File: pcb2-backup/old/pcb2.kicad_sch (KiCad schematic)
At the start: 69 parts, among them J1 WQP419GR_audio_in_1, J10 ACJS-HHOP_pedal_3, J11 ACJS-HHOP_pedal_4, J12 PMOD_JD, J13 PMOD_JC, J14 ACJS-HHOP_audio_out_L, J15 ACJS-HHOP_audio_out_R, J2 WQP419GR_audio_in_3, J3 Barrel_+5V_in, J4 Conn_+5V_to_FPGA, J5 Conn_GND_to_FPGA, J6 WQP419GR_audio_in_2, J7 WQP419GR_audio_in_4, J8 ACJS-HHOP_pedal_1, J9 ACJS-HHOP_pedal_2, U1 LM3940, U2 PCM1840, U3 ADC104S021, U4 TAD5242

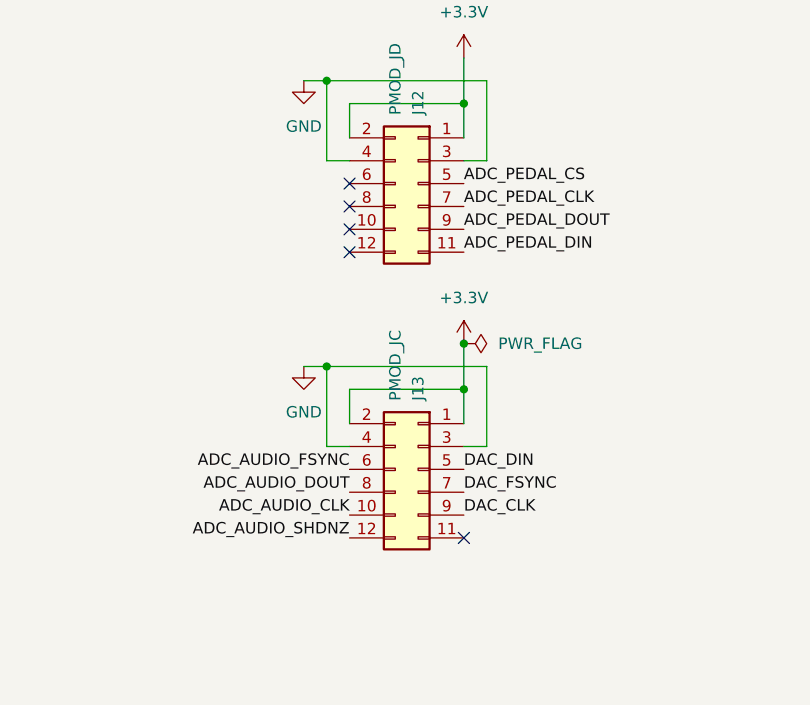
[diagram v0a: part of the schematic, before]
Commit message: Implement expression pedal controls
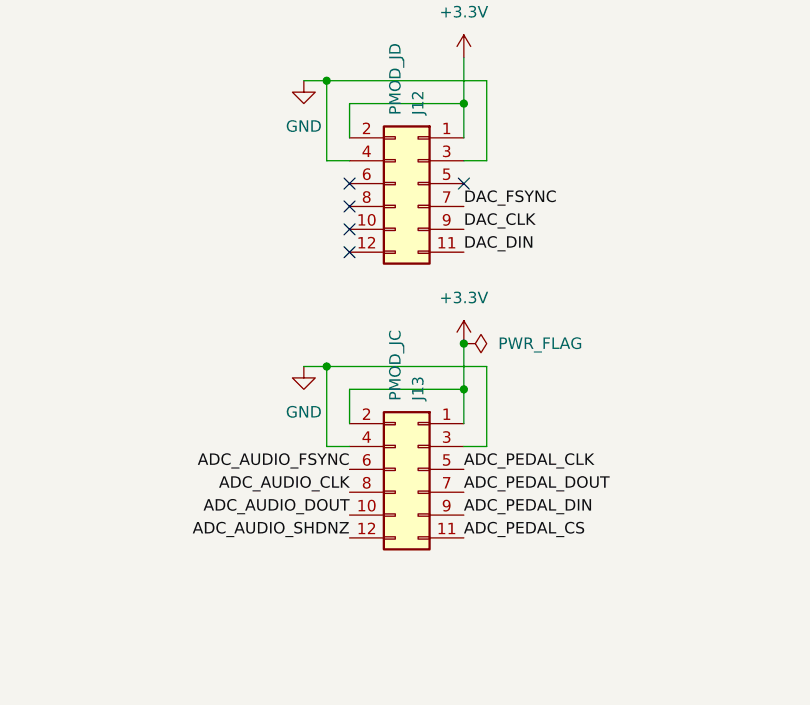
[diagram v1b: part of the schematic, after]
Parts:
- C10, C5, J1, J10, J11, J12, J13, J14, J15, J2, J3, J4, J5, J6, J7, J8, J9, U1: now in the parts list
- U3: FT Rotation Offset -90 -> (none)
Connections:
- net ADC_AUDIO_CLK: now also J13.8 (Pin_8); no longer J13.10 (Pin_10)
- net ADC_AUDIO_DOUT: now also J13.10 (Pin_10); no longer J13.8 (Pin_8)
- net ADC_PEDAL_CLK: now also J13.5 (Pin_5); no longer J12.7 (Pin_7)
- net ADC_PEDAL_CS: now also J13.11 (Pin_11); no longer J12.5 (Pin_5)
- net ADC_PEDAL_DIN: now also J13.9 (Pin_9); no longer J12.11 (Pin_11)
- net ADC_PEDAL_DOUT: now also J13.7 (Pin_7); no longer J12.9 (Pin_9)
- net DAC_CLK: now also J12.9 (Pin_9); no longer J13.9 (Pin_9)
- net DAC_DIN: now also J12.11 (Pin_11); no longer J13.5 (Pin_5)
- net DAC_FSYNC: now also J12.7 (Pin_7); no longer J13.7 (Pin_7)
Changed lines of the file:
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@@
 	)
 	(no_connect
-		(at 232.41 160.02)
+		(at 232.41 120.65)
 	)
 	(no_connect
@@
 		)
 	)
+	(label "ADC_PEDAL_CS"
+		(at 232.41 160.02 0)
+		(effects
+			(font
+				(size 1.27 1.27)
+			)
+			(justify left bottom)
+		)
+	)
 	(label "DAC_DIN"
-		(at 232.41 152.4 0)
+		(at 232.41 128.27 0)
 		(effects
 			(font
@@
 		)
 	)
-	(label "ADC_IN4N"
-		(at 100.33 148.59 0)
+	(label "ADC_PEDAL_DIN"
+		(at 232.41 157.48 0)
 		(effects
 			(font
@@
 		)
 	)
-	(label "DAC_OUT2N"
-		(at 246.38 80.01 0)
+	(label "ADC_IN4N"
+		(at 100.33 148.59 0)
 		(effects
 			(font
@@
 		)
 	)
-	(label "ADC_PEDAL_DOUT"
-		(at 166.37 46.99 0)
+	(label "ADC_PEDAL_CLK"
+		(at 232.41 152.4 0)
 		(effects
 			(font
@@
 		)
 	)
-	(label "ADC_PEDAL_CS"
-		(at 166.37 52.07 0)
+	(label "DAC_OUT2N"
+		(at 246.38 80.01 0)
 		(effects
 			(font
@@
 		)
 	)
-	(label "ADC_PEDAL_DIN"
-		(at 232.41 128.27 0)
+	(label "ADC_PEDAL_DOUT"
+		(at 166.37 46.99 0)
 		(effects
 			(font
@@
 	)
 	(label "ADC_PEDAL_CS"
-		(at 232.41 120.65 0)
+		(at 166.37 52.07 0)
 		(effects
 			(font
@@
 	)
 	(label "ADC_PEDAL_DOUT"
-		(at 232.41 125.73 0)
+		(at 232.41 154.94 0)
 		(effects
 			(font
@@
 	)
 	(label "ADC_AUDIO_CLK"
-		(at 219.71 157.48 180)
+		(at 219.71 154.94 180)
 		(effects
 			(font
@@
 	)
 	(label "DAC_FSYNC"
-		(at 232.41 154.94 0)
-		(effects
-			(font
-				(size 1.27 1.27)
-			)
-			(justify left bottom)
-		)
-	)
-	(label "ADC_PEDAL_CLK"
 		(at 232.41 123.19 0)
 		(effects
@@
 	)
 	(label "ADC_AUDIO_DOUT"
-		(at 219.71 154.94 180)
+		(at 219.71 157.48 180)
 		(effects
 			(font
@@
 	)
 	(label "DAC_CLK"
-		(at 232.41 157.48 0)
+		(at 232.41 125.73 0)
 		(effects
 			(font
@@
 		(body_style 1)
 		(exclude_from_sim no)
-		(in_bom no)
+		(in_bom yes)
 		(on_board yes)
-		(in_pos_files no)
+		(in_pos_files yes)
 		(dnp no)
 		(property "Reference" "J11"
@@
 		(body_style 1)
 		(exclude_from_sim no)
-		(in_bom no)
+		(in_bom yes)
 		(on_board yes)
-		(in_pos_files no)
+		(in_pos_files yes)
 		(dnp no)
 		(fields_autoplaced yes)
@@
 		(body_style 1)
 		(exclude_from_sim no)
-		(in_bom no)
+		(in_bom yes)
 		(on_board yes)
-		(in_pos_files no)
+		(in_pos_files yes)
 		(dnp no)
 		(property "Reference" "J4"
@@
 		(body_style 1)
 		(exclude_from_sim no)
-		(in_bom no)
+		(in_bom yes)
 		(on_board yes)
-		(in_pos_files no)
+		(in_pos_files yes)
 		(dnp no)
 		(fields_autoplaced yes)
@@
 		(body_style 1)
 		(exclude_from_sim no)
-		(in_bom no)
+		(in_bom yes)
 		(on_board yes)
-		(in_pos_files no)
+		(in_pos_files yes)
 		(dnp no)
 		(property "Reference" "J1"
@@
 		(body_style 1)
 		(exclude_from_sim no)
-		(in_bom no)
+		(in_bom yes)
 		(on_board yes)
-		(in_pos_files no)
+		(in_pos_files yes)
 		(dnp no)
 		(property "Reference" "J10"
@@
 		(body_style 1)
 		(exclude_from_sim no)
-		(in_bom no)
+		(in_bom yes)
 		(on_board yes)
-		(in_pos_files no)
+		(in_pos_files yes)
 		(dnp no)
 		(property "Reference" "J8"
@@
 		(body_style 1)
 		(exclude_from_sim no)
-		(in_bom no)
+		(in_bom yes)
 		(on_board yes)
-		(in_pos_files no)
+		(in_pos_files yes)
 		(dnp no)
 		(property "Reference" "J5"
@@
 		(body_style 1)
 		(exclude_from_sim no)
-		(in_bom no)
+		(in_bom yes)
 		(on_board yes)
-		(in_pos_files no)
+		(in_pos_files yes)
 		(dnp no)
 		(property "Reference" "J7"
@@
 		(body_style 1)
 		(exclude_from_sim no)
-		(in_bom no)
+		(in_bom yes)
 		(on_board yes)
-		(in_pos_files no)
+		(in_pos_files yes)
 		(dnp no)
 		(fields_autoplaced yes)
@@
 		(body_style 1)
 		(exclude_from_sim no)
-		(in_bom no)
+		(in_bom yes)
 		(on_board yes)
-		(in_pos_files no)
+		(in_pos_files yes)
 		(dnp no)
 		(property "Reference" "J15"
@@
 		(body_style 1)
 		(exclude_from_sim no)
-		(in_bom no)
+		(in_bom yes)
 		(on_board yes)
-		(in_pos_files no)
+		(in_pos_files yes)
 		(dnp no)
 		(property "Reference" "J13"
@@
 		(body_style 1)
 		(exclude_from_sim no)
-		(in_bom no)
+		(in_bom yes)
 		(on_board yes)
-		(in_pos_files no)
+		(in_pos_files yes)
 		(dnp no)
 		(property "Reference" "J9"
@@
 		(body_style 1)
 		(exclude_from_sim no)
-		(in_bom no)
+		(in_bom yes)
 		(on_board yes)
-		(in_pos_files no)
+		(in_pos_files yes)
 		(dnp no)
 		(property "Reference" "J2"
@@
 		(body_style 1)
 		(exclude_from_sim no)
-		(in_bom no)
+		(in_bom yes)
 		(on_board yes)
-		(in_pos_files no)
+		(in_pos_files yes)
 		(dnp no)
 		(property "Reference" "J12"
@@
 		(body_style 1)
 		(exclude_from_sim no)
-		(in_bom no)
+		(in_bom yes)
 		(on_board yes)
-		(in_pos_files no)
+		(in_pos_files yes)
 		(dnp no)
 		(property "Reference" "J14"
@@
 		(body_style 1)
 		(exclude_from_sim no)
-		(in_bom no)
+		(in_bom yes)
 		(on_board yes)
-		(in_pos_files no)
+		(in_pos_files yes)
 		(dnp no)
 		(fields_autoplaced yes)
@@
 		(body_style 1)
 		(exclude_from_sim no)
-		(in_bom no)
+		(in_bom yes)
 		(on_board yes)
-		(in_pos_files no)
+		(in_pos_files yes)
 		(dnp no)
 		(property "Reference" "J6"
@@
 			(at 157.48 48.26 0)
 			(hide yes)
-			(show_name no)
-			(do_not_autoplace no)
-			(effects
-				(font
-					(size 1.27 1.27)
-				)
-			)
-		)
-		(property "FT Rotation Offset" "-90"
-			(at 157.48 48.26 0)
-			(hide yes)
